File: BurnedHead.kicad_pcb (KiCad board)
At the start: 4 copper layers, 121.9 x 44.4 mm, 90 parts, among them J1 USB_B_Micro, J2 Conn_ARM_JTAG_SWD_10, J3 DM3AT-SF-PEJMS, J4 FPC_1x5_TopContact_P=0.5mm, J5 FPC_1x5_TopContact_P=0.5mm, Q2 IRLML6401TRPBF, SW1 SW_SPDT, SW2 SW_Push, SW3 SW_Push, SW4 DualShock-DPad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

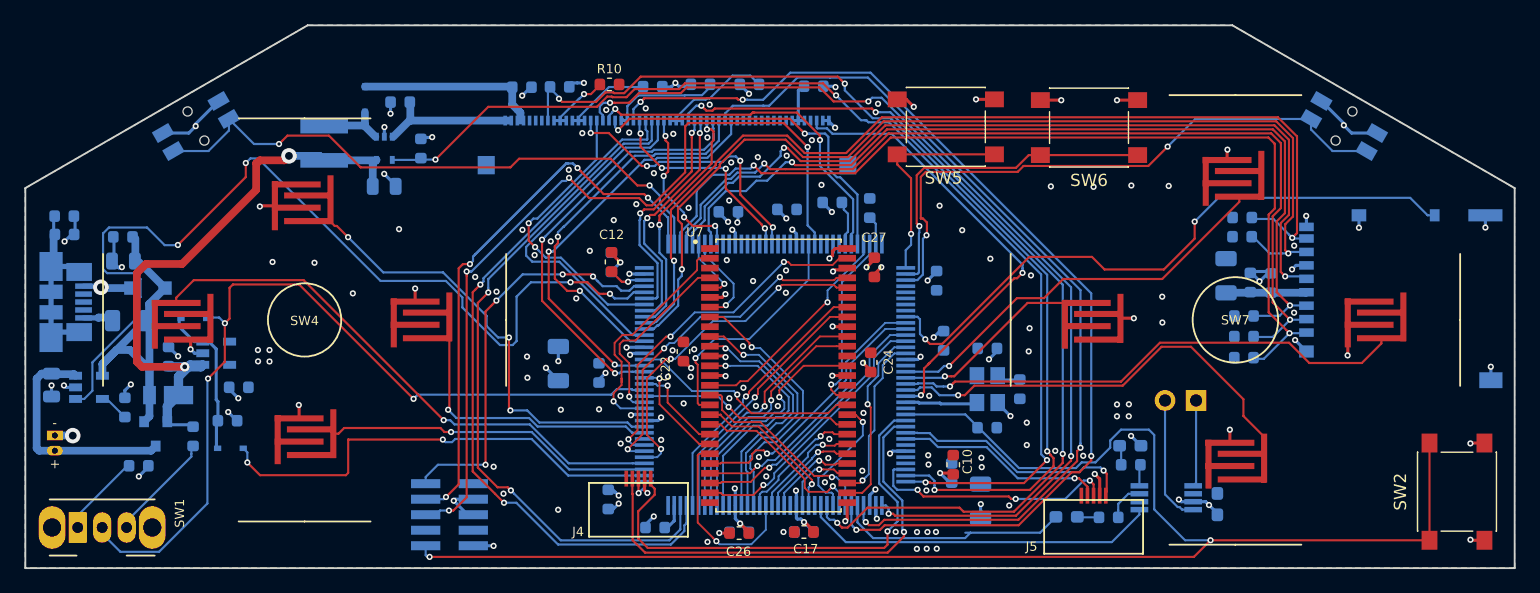
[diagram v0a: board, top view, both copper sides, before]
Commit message: Add capacitor to lcd vdd and one more to ram vdd pin, updating parts-lib
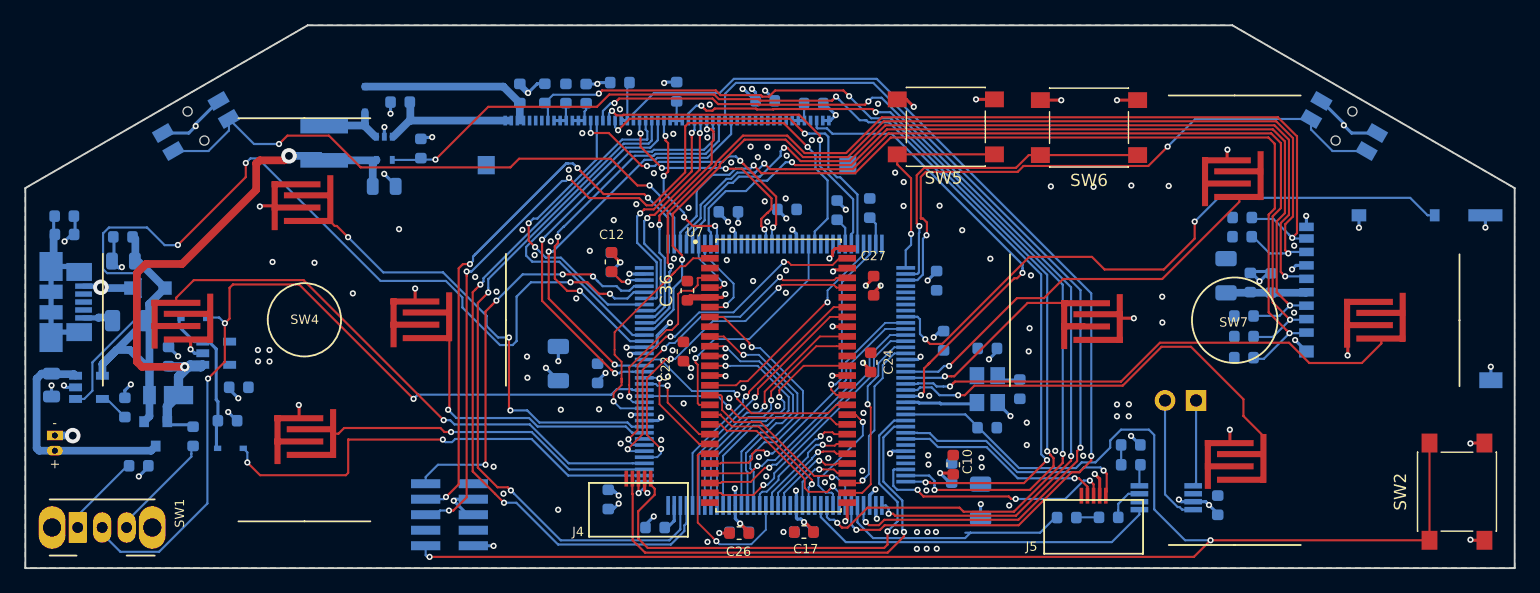
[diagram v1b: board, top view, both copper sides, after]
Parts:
- added C35: C100nF, Capacitor_SMD:C_0603_1608Metric, B.Cu at (214.9, 144.0)
- added C36: C100nF, Capacitor_SMD:C_0603_1608Metric, F.Cu at (208.5, 159.5)
- C32, C33, C34: footprint Capacitor_SMD:C_0603_1608Metric_Pad1.05x0.95mm_HandSolder -> Capacitor_SMD:C_0603_1608Metric
- R10: moved to B.Cu
- moved R16 6.60 mm to (203.0, 142.5)
- moved R17 5.98 mm to (207.6, 143.2), turned to 270 degrees
- moved R15 5.48 mm to (200.2, 143.4), turned to 270 degrees
- moved R10 3.65 mm to (198.6, 143.4), turned to 90 degrees
- moved C27 1.51 mm to (223.7, 159.1)
- moved R11 1.41 mm to (218.8, 144.2)
- moved R9 1.33 mm to (196.8, 143.4), turned to 90 degrees
- moved R13 0.74 mm to (220.8, 152.9), turned to 270 degrees
- moved C7 0.54 mm to (194.8, 143.4), turned to 90 degrees
- moved C23 0.12 mm to (201.2, 166.3)
- moved C34 0.09 mm to (251.9, 177.1)
- moved C32 0.08 mm to (244.8, 172.2)
- moved SW7 0.06 mm to (253.3, 162.0)
- moved C33 0.06 mm to (239.6, 178.1)
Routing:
- net /LCD/LCD_R0: track 9.75 -> 2.59 mm
- net /VDD: track 10.8 -> 16.9 mm, vias 59 -> 65
- net /LCD/LCD_G0: track 9.55 -> 4.52 mm
- net /LCD/LCD_B0: track 7.33 -> 2.47 mm
- net GNDD: track 166.5 -> 169.9 mm, vias 141 -> 143
- net Net-(R10-Pad1): track 5.47 -> 2.44 mm, vias 1 -> 0
- net /LCD/LCD_NRESET: track 82.0 -> 79.5 mm
- net /LCD/LCD_G3: track 17.4 -> 18.9 mm
- net Net-(R11-Pad1): track 3.87 -> 2.41 mm
- net Net-(R13-Pad2): track 3.64 -> 2.26 mm
- net /LCD/LCD_B5: track 79.7 -> 78.6 mm
- net /MCU/SWO: track 68.4 -> 69.3 mm
- net /LCD/LCD_G2: track 84.7 -> 83.9 mm, vias 4 -> 2
- net /LCD/LCD_VSYNC: track 73.3 -> 73.8 mm
- net /LCD/LCD_DIM: track 90.2 -> 89.7 mm

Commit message: Remove accidental slots on ground plane from adjacent vias, add rev to silkscreen, re-generate gerbers
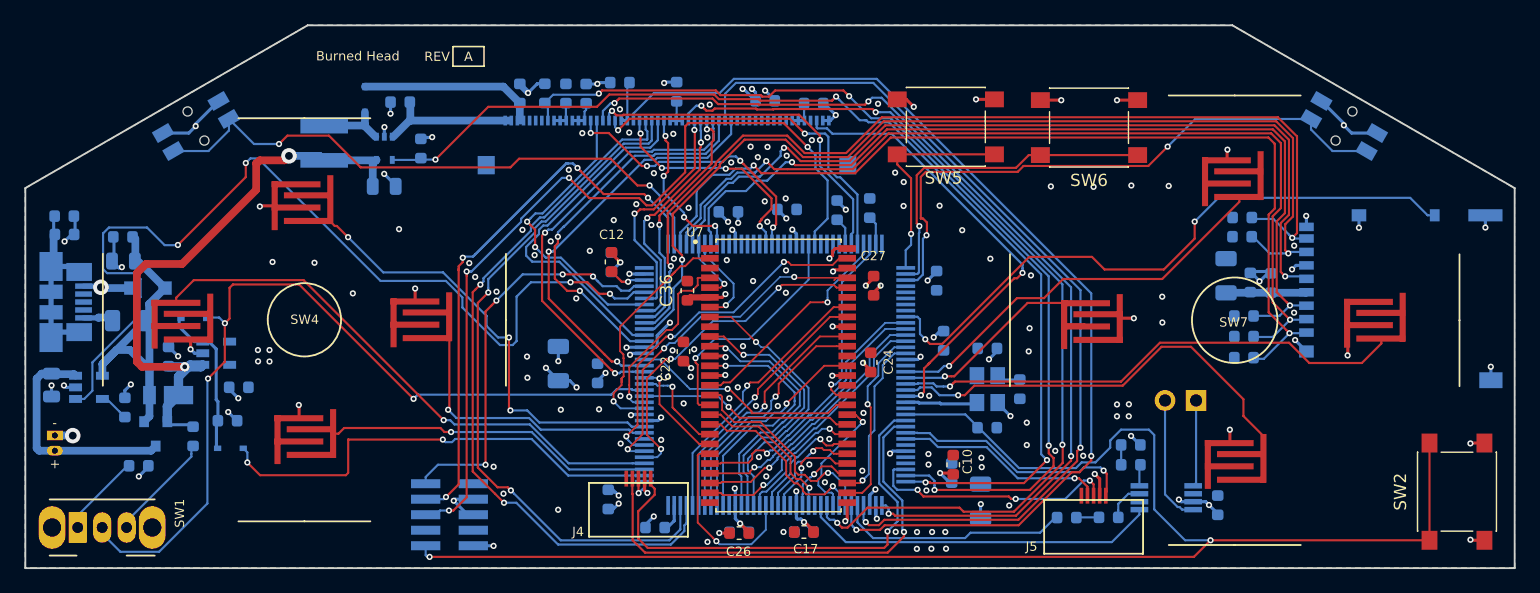
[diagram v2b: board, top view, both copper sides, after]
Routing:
- net /VDD: track 16.9 -> 18.6 mm, vias 65 -> 66
- net /MCU/D8: track 19.4 -> 17.9 mm
- net /MCU/SDNWE: track 16.4 -> 17.7 mm
- net /MCU/D5: track 20.7 -> 21.8 mm
- net /MCU/D6: track 19.8 -> 21.0 mm
- net /MCU/D14: track 28.5 -> 29.5 mm
- net /MCU/D7: track 19.6 -> 20.6 mm
- net /MCU/D4: track 22.1 -> 22.9 mm
- net /MCU/A9: track 9.10 -> 9.83 mm
- net /MCU/A7: track 7.45 -> 8.18 mm
- net /MCU/A8: track 8.31 -> 9.03 mm
- net /MCU/A11: track 10.4 -> 11.0 mm
- net /MCU/SDNCS: track 14.8 -> 15.3 mm
- net GNDD: vias 143 -> 144
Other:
- board text added: "A"
- board text added: "Burned Head"
- board text added: "REV"
